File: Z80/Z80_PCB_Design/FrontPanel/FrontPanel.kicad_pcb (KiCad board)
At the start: 2 copper layers, 95 x 95 mm, 116 parts, among them J1 Conn_01x02, J2 CONN_4, J3 CONN_4, J6 CONN_02X02, SW1 SW_Push, SW10 SW_Push, SW11 SW_Push, SW12 SW_Push, SW13 SW_Push, SW14 SW_Push, SW15 SW_Push, SW16 SW_Push, SW17 SW_Push, SW18 SW_Push, SW19 SW_Push, SW2 SW_Push, SW20 SW_Push, SW21 SW_Push, SW22 SW_Push, SW23 SW_Push, SW24 SW_Push, SW25 SW_Push, SW26 SW_Push, SW27 SW_Push, SW28 SW_Push, SW29 SW_Push, SW3 SW_Push, SW30 SW_Push, SW31 SW_Push, SW32 SW_Push, SW4 SW_Push, SW5 SW_Push, SW6 SW_Push, SW7 SW_Push, SW8 SW_Push, SW9 SW_Push, U1 MCP23017-E/SS, U2 MCP23017-E/SS, U3 MCP23017-E/SS, U4 MCP23017-E/SS

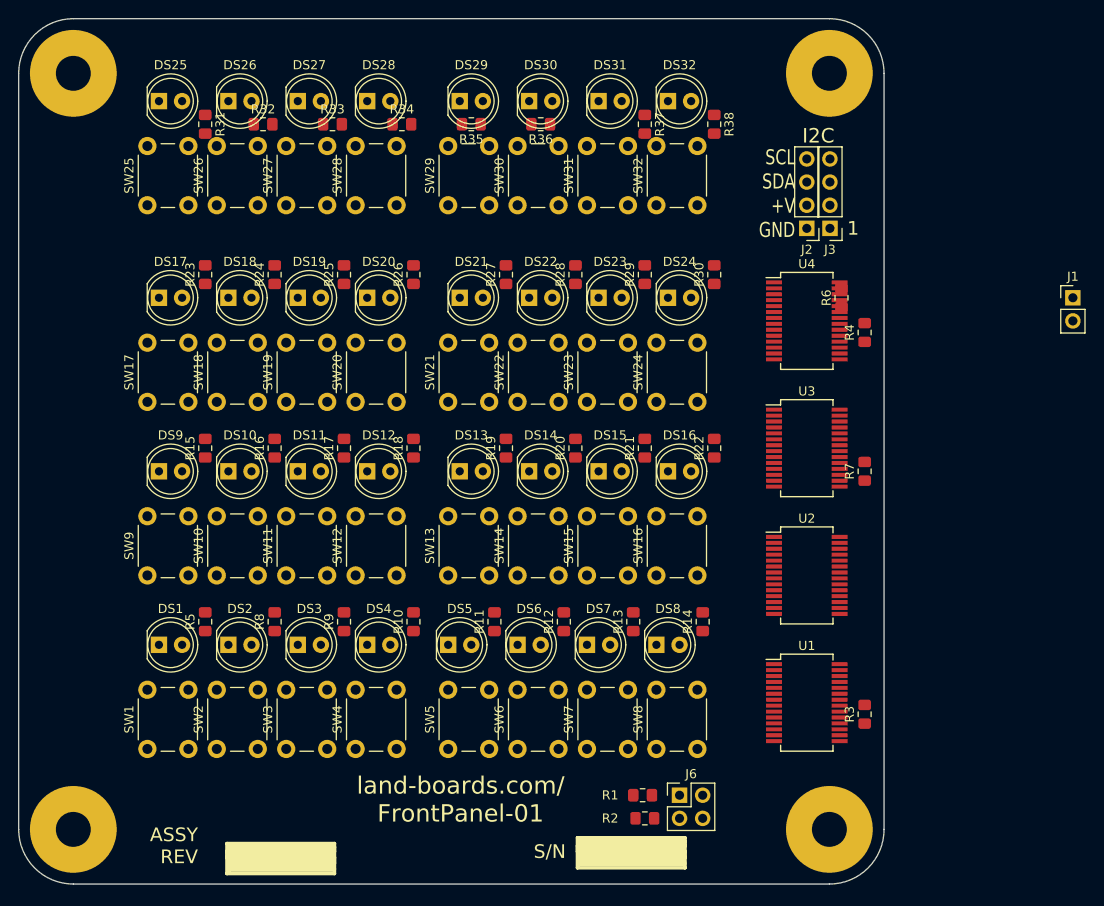
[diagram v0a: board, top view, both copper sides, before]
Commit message: Front panel design
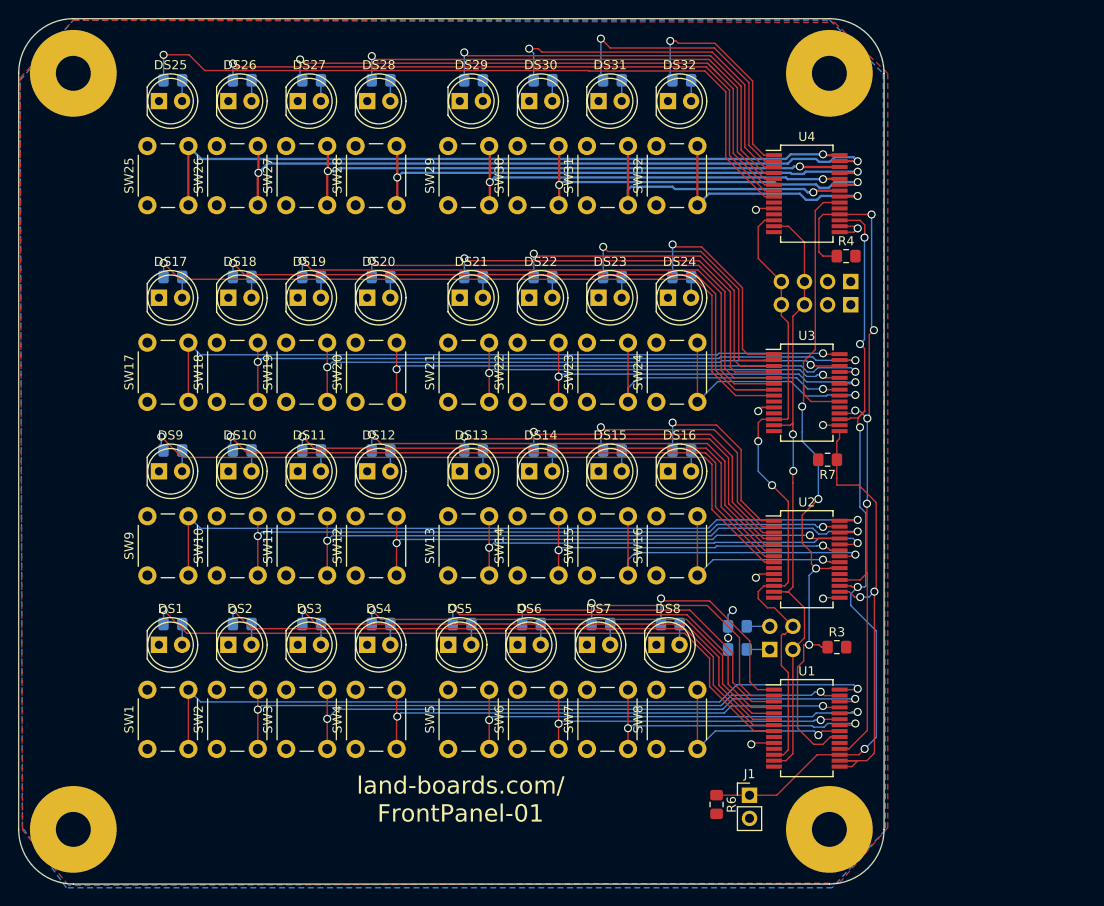
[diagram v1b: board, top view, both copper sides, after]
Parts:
- removed ST1, ST2: CONN_1, REV_BLOCK
- J2, J3, J6, R1, R10, R11, R12, R13, R14, R15, R16, R17, R18, R19, R2, R20, R21, R22, R23, R24, R25, R26, R27, R28, R29, R30, R31, R32, R33, R34, R35, R36, R37, R38, R5, R8, R9: moved to B.Cu
- moved J1 65.1 mm to (90.2, 95.2)
- moved R6 57.3 mm to (86.6, 96.3), turned to 270 degrees
- moved R2 23.4 mm to (88.9, 76.7)
- moved R1 19.1 mm to (88.9, 79.2)
- moved J6 18.8 mm to (92.5, 79.2)
- moved U4 14.0 mm to (96.5, 29.2)
- moved J2 9.67 mm to (101.3, 41.4), turned to 90 degrees
- moved R4 8.62 mm to (100.8, 36.1), turned to 0 degrees
- moved R3 7.97 mm to (99.8, 79.0), turned to 0 degrees
- moved J3 6.27 mm to (101.3, 38.9), turned to 90 degrees
- moved U3 6.10 mm to (96.5, 51.1)
- moved R31 5.99 mm to (26.9, 16.8), turned to 180 degrees
- moved R37 5.99 mm to (75.2, 16.8), turned to 180 degrees
- moved R38 5.99 mm to (82.8, 16.8), turned to 180 degrees
- moved R32 5.34 mm to (34.5, 16.8), turned to 180 degrees
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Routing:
- net /A2: track 0.00 -> 88.0 mm, vias 0 -> 5
- net /S1D7: track 0.00 -> 83.5 mm, vias 0 -> 1
- net /S2D7: track 0.00 -> 82.9 mm, vias 0 -> 1
- net Net-(R31-Pad2): track 0.00 -> 80.5 mm, vias 0 -> 1
- net /PUPRST: track 0.00 -> 79.7 mm, vias 0 -> 5
- net Net-(R23-Pad2): track 0.00 -> 79.5 mm, vias 0 -> 1
- net /PUPINT: track 0.00 -> 79.4 mm, vias 0 -> 4
- net /S4D7: track 0.00 -> 78.8 mm, vias 0 -> 1
- net /S3D7: track 0.00 -> 78.6 mm, vias 0 -> 1
- net Net-(R15-Pad2): track 0.00 -> 77.5 mm, vias 0 -> 1
- net Net-(R5-Pad2): track 0.00 -> 75.9 mm, vias 0 -> 1
- net Net-(R24-Pad2): track 0.00 -> 75.7 mm, vias 0 -> 1
- net /S4D6: track 0.00 -> 75.5 mm, vias 0 -> 2
- net /S3D6: track 0.00 -> 74.2 mm, vias 0 -> 2
- net /SCL: track 0.00 -> 72.7 mm, vias 0 -> 2
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- added copper zone on F.Cu, net +5V
- added copper zone on B.Cu, net GND
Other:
- rule trace_min: 0.254 -> 0.1524
- board text added: "PWB Rev 1"
- board text removed: "ASSY REV"
- board text removed: "PWB Rev X4"
- board text removed: "S/N"

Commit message: Added I2C interface to Z80 CPU
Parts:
- added TEST: CONN_1, LandBoards_Marking:TEST_BLK-REAR, F.Cu at (15.8, 86.8)
- J1: moved to B.Cu
- J2: value CONN_4 -> Conn_01x05; footprint Connector_PinHeader_2.54mm:PinHeader_1x04_P2.54mm_Vertical -> Connector_PinHeader_2.54mm:PinHeader_1x05_P2.54mm_Vertical
- moved R3 2.26 mm to (99.7, 81.3), turned to 180 degrees
- moved DS6 1.27 mm to (66.0, 78.7)
- moved DS5 1.27 mm to (58.4, 78.7)
- moved DS7 1.27 mm to (73.7, 78.7)
- moved DS8 1.27 mm to (81.3, 78.7)
- moved R12 1.02 mm to (67.3, 76.5)
- moved R13 1.02 mm to (74.9, 76.5)
- moved R11 1.02 mm to (59.7, 76.5)
- moved R14 1.02 mm to (82.5, 76.5)
- moved R1 0.13 mm to (88.9, 79.4)
- moved R2 0.13 mm to (88.9, 76.8)
- turned R4 to 180 degrees
- turned R7 to 0 degrees
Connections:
- R3 pad 1: /PUPINT -> +5V
- R3 pad 2: +5V -> /PUPINT
- R4 pad 1: /PUPRST -> +5V
- R4 pad 2: +5V -> /PUPRST
- R7 pad 1: /PUPADR -> +5V
- R7 pad 2: +5V -> /PUPADR
- U1 pad 19: (no net) -> /PUPINT
- U2 pad 19: (no net) -> /PUPINT
- U3 pad 19: (no net) -> /PUPINT
- U4 pad 19: (no net) -> /PUPINT
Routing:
- net /PUPINT: track 79.4 -> 100.1 mm, vias 4 -> 5
- net Net-(R14-Pad2): track 22.0 -> 24.6 mm, vias 1 -> 2
- net Net-(R13-Pad2): track 29.5 -> 31.6 mm
- net Net-(R10-Pad2): track 52.2 -> 53.8 mm
- net Net-(R9-Pad2): track 60.1 -> 61.7 mm
- net Net-(R8-Pad2): track 68.0 -> 69.5 mm
- net +5V: track 4.54 -> 5.77 mm, vias 2 -> 1
- net Net-(R5-Pad2): track 75.9 -> 77.0 mm
- net /S1D1: track 33.6 -> 34.4 mm, vias 2 -> 1
- net /A2: track 88.0 -> 88.8 mm
- net Net-(R12-Pad2): track 35.6 -> 36.2 mm
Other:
- net class Default: clearance 0.254 -> 0.1524; trace_width 0.254 -> 0.1524
- rule trace_clearance: 0.254 -> 0.1524
- board text added: "A2"
- board text added: "I2C> TERMS>"
- board text added: "land-boards.com/FrontPanel-01"
- board text added: "~INT SCL SDA +V GND"
- board text removed: "SCL SDA +V GND"
- board text removed: "land-boards.com/ FrontPanel-01"
